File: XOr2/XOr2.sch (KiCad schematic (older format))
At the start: 13 parts, among them J1 In1, J2 In2, J3 Out, J4 Thru1, J5 Thru2

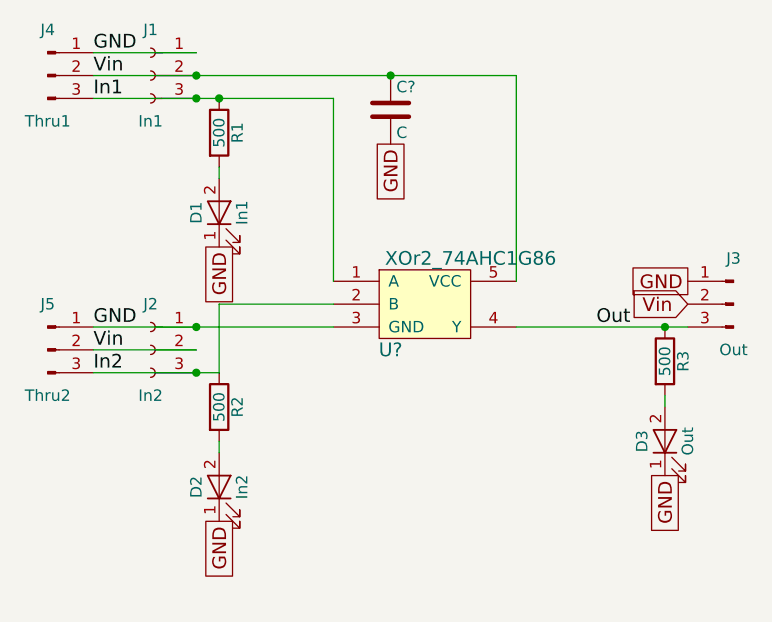
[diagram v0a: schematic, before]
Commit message: Made XOR Board and modified FA
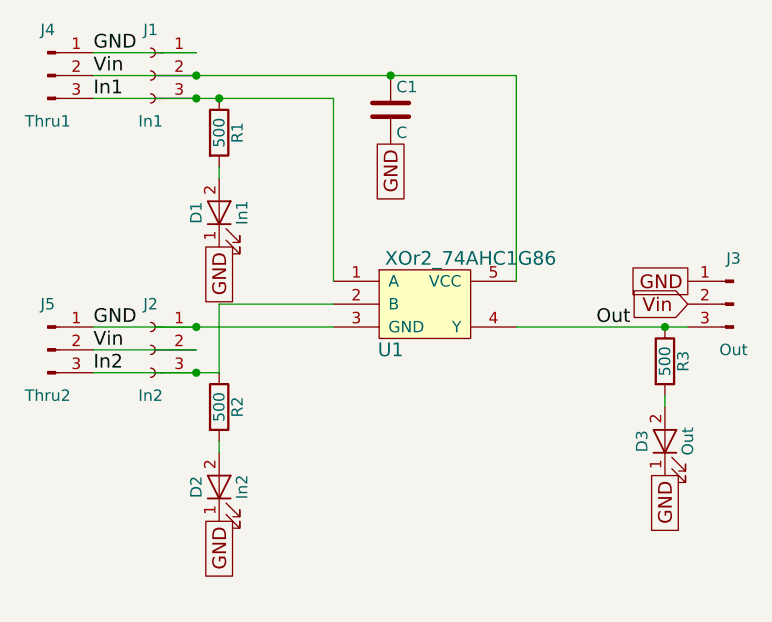
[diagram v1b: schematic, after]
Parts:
- C1: renamed from C?; footprint (none) -> Capacitors_SMD:C_0603_HandSoldering
- D1, D2, D3: footprint (none) -> LEDs:LED_0603_HandSoldering
- J1, J2: footprint (none) -> Socket_Strips:Socket_Strip_Angled_1x03_Pitch2.54mm
- J3, J4, J5: footprint (none) -> Pin_Headers:Pin_Header_Angled_1x03_Pitch2.54mm
- R1, R2, R3: footprint (none) -> Resistors_SMD:R_0603_HandSoldering
- U1: renamed from U?; footprint (none) -> Logic Blocks:SC_70_1.25mm
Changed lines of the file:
@@
 F 0 "J3" H 6900 4650 50  0000 C CNN
 F 1 "Out" H 6900 4250 50  0000 C CNN
-F 2 "" H 6900 4450 50  0001 C CNN
+F 2 "Pin_Headers:Pin_Header_Angled_1x03_Pitch2.54mm" H 6900 4450 50  0001 C CNN
 F 3 "" H 6900 4450 50  0001 C CNN
 	1    6900 4450
@@
 F 0 "J1" H 4350 3650 50  0000 C CNN
 F 1 "In1" H 4350 3250 50  0000 C CNN
-F 2 "" H 4350 3450 50  0001 C CNN
+F 2 "Socket_Strips:Socket_Strip_Angled_1x03_Pitch2.54mm" H 4350 3450 50  0001 C CNN
 F 3 "" H 4350 3450 50  0001 C CNN
 	1    4350 3450
@@
 F 0 "J2" H 4350 4850 50  0000 C CNN
 F 1 "In2" H 4350 4450 50  0000 C CNN
-F 2 "" H 4350 4650 50  0001 C CNN
+F 2 "Socket_Strips:Socket_Strip_Angled_1x03_Pitch2.54mm" H 4350 4650 50  0001 C CNN
 F 3 "" H 4350 4650 50  0001 C CNN
 	1    4350 4650
@@
 F 0 "J5" H 3900 4850 50  0000 C CNN
 F 1 "Thru2" H 3900 4450 50  0000 C CNN
-F 2 "" H 3900 4650 50  0001 C CNN
+F 2 "Pin_Headers:Pin_Header_Angled_1x03_Pitch2.54mm" H 3900 4650 50  0001 C CNN
 F 3 "" H 3900 4650 50  0001 C CNN
 	1    3900 4650
@@
 F 0 "J4" H 3900 3650 50  0000 C CNN
 F 1 "Thru1" H 3900 3250 50  0000 C CNN
-F 2 "" H 3900 3450 50  0001 C CNN
+F 2 "Pin_Headers:Pin_Header_Angled_1x03_Pitch2.54mm" H 3900 3450 50  0001 C CNN
 F 3 "" H 3900 3450 50  0001 C CNN
 	1    3900 3450
@@
 F 0 "D2" H 4650 5350 50  0000 C CNN
 F 1 "In2" H 4650 5150 50  0000 C CNN
-F 2 "" H 4650 5250 50  0001 C CNN
+F 2 "LEDs:LED_0603_HandSoldering" H 4650 5250 50  0001 C CNN
 F 3 "" H 4650 5250 50  0001 C CNN
 	1    4650 5250
@@
 F 0 "R2" V 4730 4900 50  0000 C CNN
 F 1 "500" V 4650 4900 50  0000 C CNN
-F 2 "" V 4580 4900 50  0001 C CNN
+F 2 "Resistors_SMD:R_0603_HandSoldering" V 4580 4900 50  0001 C CNN
 F 3 "" H 4650 4900 50  0001 C CNN
 	1    4650 4900
@@
 F 0 "D1" H 4650 4150 50  0000 C CNN
 F 1 "In1" H 4650 3950 50  0000 C CNN
-F 2 "" H 4650 4050 50  0001 C CNN
+F 2 "LEDs:LED_0603_HandSoldering" H 4650 4050 50  0001 C CNN
 F 3 "" H 4650 4050 50  0001 C CNN
 	1    4650 4050
@@
 F 0 "D3" H 6600 5150 50  0000 C CNN
 F 1 "Out" H 6600 4950 50  0000 C CNN
-F 2 "" H 6600 5050 50  0001 C CNN
+F 2 "LEDs:LED_0603_HandSoldering" H 6600 5050 50  0001 C CNN
 F 3 "" H 6600 5050 50  0001 C CNN
 	1    6600 5050
@@
 F 0 "R3" V 6680 4700 50  0000 C CNN
 F 1 "500" V 6600 4700 50  0000 C CNN
-F 2 "" V 6530 4700 50  0001 C CNN
+F 2 "Resistors_SMD:R_0603_HandSoldering" V 6530 4700 50  0001 C CNN
 F 3 "" H 6600 4700 50  0001 C CNN
 	1    6600 4700
@@
 F 0 "R1" V 4730 3700 50  0000 C CNN
 F 1 "500" V 4650 3700 50  0000 C CNN
-F 2 "" V 4580 3700 50  0001 C CNN
+F 2 "Resistors_SMD:R_0603_HandSoldering" V 4580 3700 50  0001 C CNN
 F 3 "" H 4650 3700 50  0001 C CNN
 	1    4650 3700
@@
 Out
 $Comp
-L XOr2_74AHC1G86 U?
+L XOr2_74AHC1G86 U1
 U 1 1 5AF1E426
 P 5350 4600
-F 0 "U?" H 5400 4550 60  0000 C CNN
+F 0 "U1" H 5400 4550 60  0000 C CNN
 F 1 "XOr2_74AHC1G86" H 5750 4950 60  0000 C CNN
-F 2 "" H 5150 4250 60  0001 C CNN
+F 2 "Logic Blocks:SC_70_1.25mm" H 5150 4250 60  0001 C CNN
 F 3 "" H 5150 4250 60  0001 C CNN
 	1    5350 4600
@@
 Connection ~ 4550 3450
 $Comp
-L C C?
+L C C1
 U 1 1 5AF1E54F
 P 5400 3600
-F 0 "C?" H 5425 3700 50  0000 L CNN
+F 0 "C1" H 5425 3700 50  0000 L CNN
 F 1 "C" H 5425 3500 50  0000 L CNN
-F 2 "" H 5438 3450 50  0001 C CNN
+F 2 "Capacitors_SMD:C_0603_HandSoldering" H 5438 3450 50  0001 C CNN
 F 3 "" H 5400 3600 50  0001 C CNN
 	1    5400 3600
